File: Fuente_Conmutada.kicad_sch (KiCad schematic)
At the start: 47 parts, among them J1 Terminal_220v, J2 Terminal_12v, J3 Vout, Q1 IRF840, Q2 IRF840, T1 Transformer_1P_SS, U1 TL494, U2 IR2110

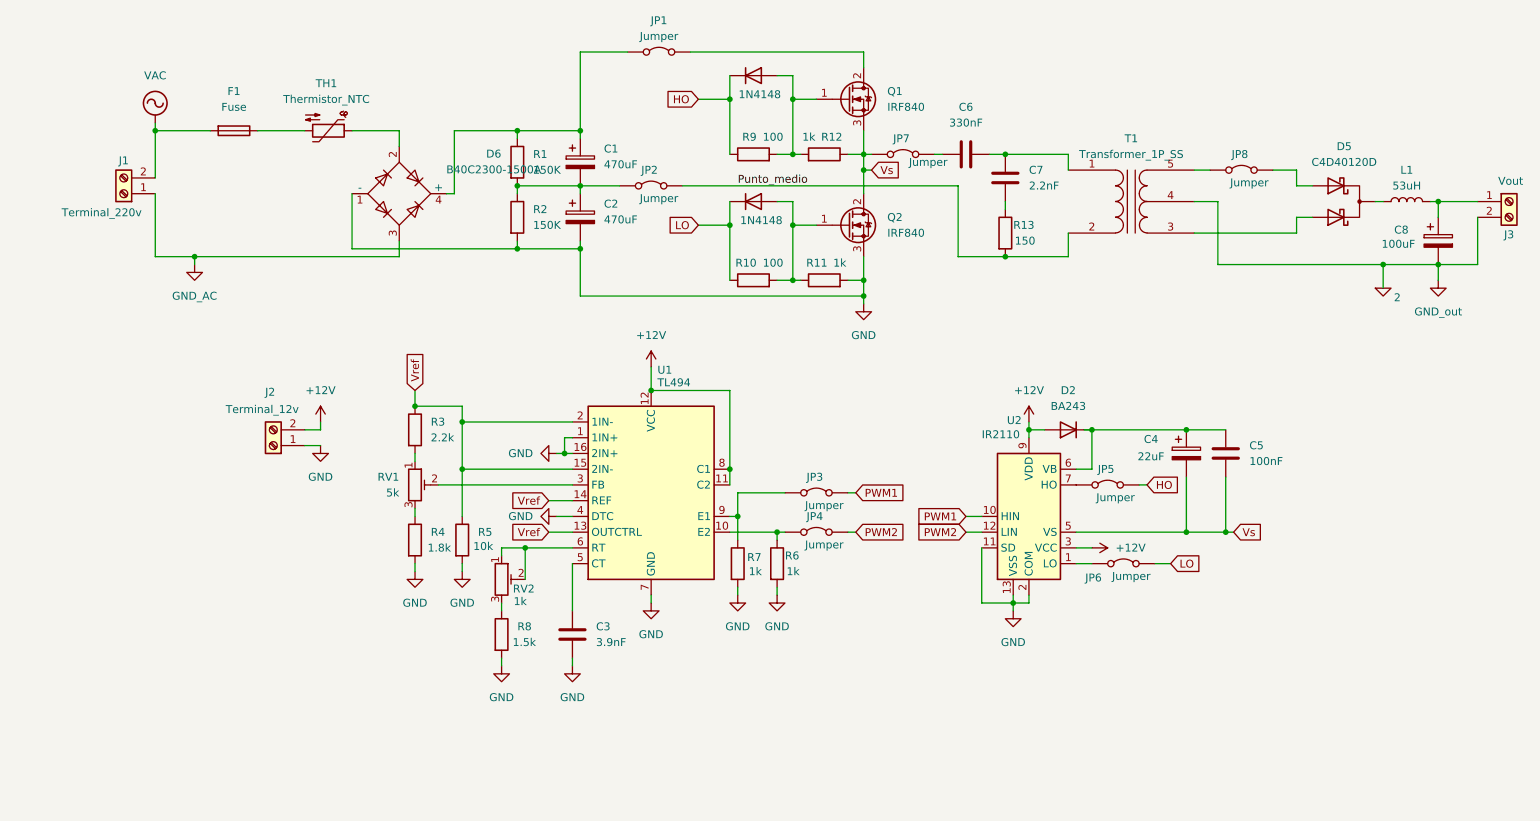
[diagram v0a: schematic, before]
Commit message: Agregado de cosas
Se agregó:
- Pads de montaje
- Footprints de disipadores para mosfets y rectificador de salida
- Se puso en la capa correcta el choke de salida
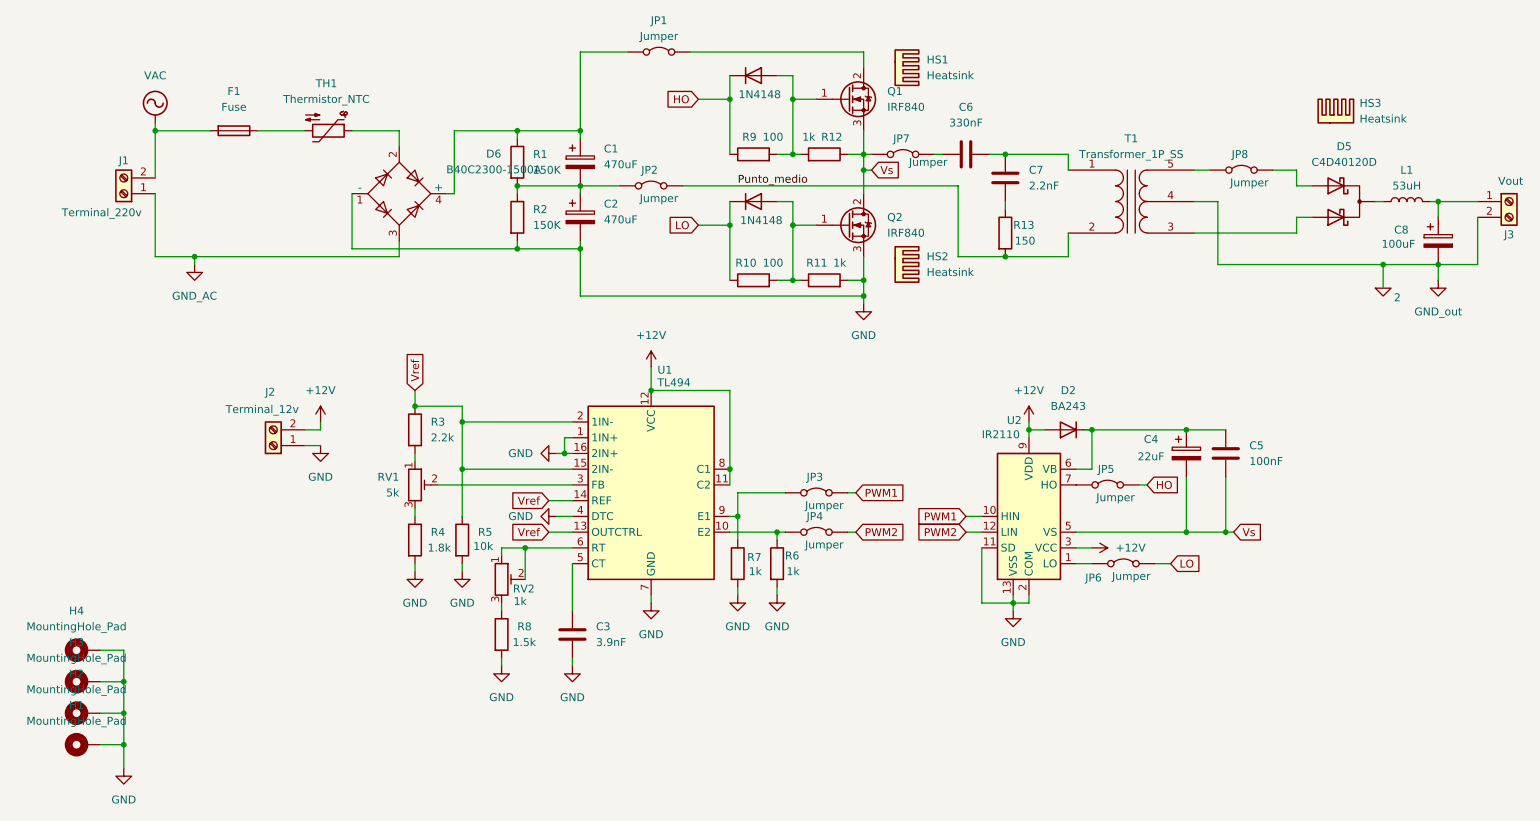
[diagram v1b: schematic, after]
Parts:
- added H1, H2, H3, H4: MountingHole_Pad, MountingHole:MountingHole_3.2mm_M3_Pad_Via, symbol Mechanical:MountingHole_Pad
- added HS1, HS2, HS3: Heatsink, Heatsink:Heatsink_Stonecold_HS-S01_13.21x6.35mm, symbol Mechanical:Heatsink
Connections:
- net GND: now also H1.1, H2.1, H3.1, H4.1
